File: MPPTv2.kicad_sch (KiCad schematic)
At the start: 11 parts

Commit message: Major
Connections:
- net GND renamed Earth
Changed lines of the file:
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@@
     )
   )
-  (symbol (lib_id "power:GND") (at 129.54 114.3 0) (unit 1)
+  (symbol (lib_id "power:Earth") (at 129.54 114.3 0) (unit 1)
     (in_bom yes) (on_board yes) (dnp no) (fields_autoplaced)
-    (property "Reference" "#PWR?" (at 129.54 120.65 0)
+    (property "Reference" "#PWR01" (at 129.54 120.65 0)
       (effects (font (size 1.27 1.27)) hide)
     )
-    (property "Value" "GND" (at 129.54 119.38 0)
-      (effects (font (size 1.27 1.27)))
+    (property "Value" "Earth" (at 129.54 118.11 0)
+      (effects (font (size 1.27 1.27)) hide)
     )
     (property "Footprint" "" (at 129.54 114.3 0)
       (effects (font (size 1.27 1.27)) hide)
     )
-    (property "Datasheet" "" (at 129.54 114.3 0)
+    (property "Datasheet" "~" (at 129.54 114.3 0)
       (effects (font (size 1.27 1.27)) hide)
     )
     (pin "1")
     (instances
-      (project "FinalBoardCircuits"
-        (path "/7d53e764-a8df-4c50-9cab-d1a3d013fedc/279ce73a-fd26-44c2-9e74-8d0dda75d83d"
-          (reference "#PWR?") (unit 1)
+      (project "pcb"
+        (path "/a8bac665-9e81-4c8d-8e7f-b88478edfeaf/df4161cb-a58b-4c44-b758-adc32db84b1a"
+          (reference "#PWR01") (unit 1)
         )
       )
-      (project "pcb"
-        (path "/a8bac665-9e81-4c8d-8e7f-b88478edfeaf/df4161cb-a58b-4c44-b758-adc32db84b1a"
-          (reference "#PWR03") (unit 1)
-        )
-      )

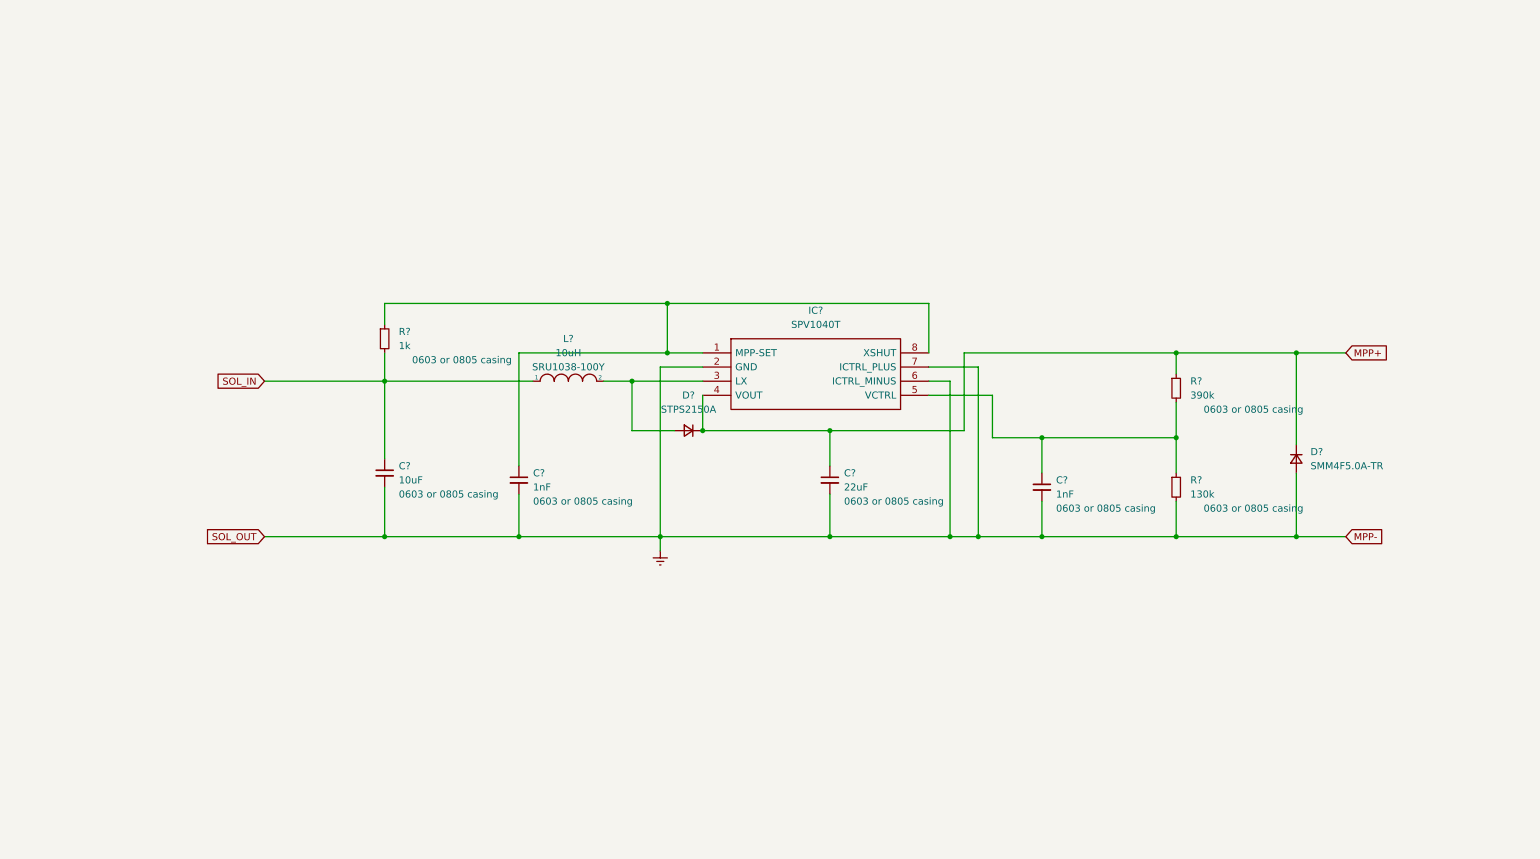
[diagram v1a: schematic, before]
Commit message: Final Schematic
Final Schematic. PC104 pins not assigned.
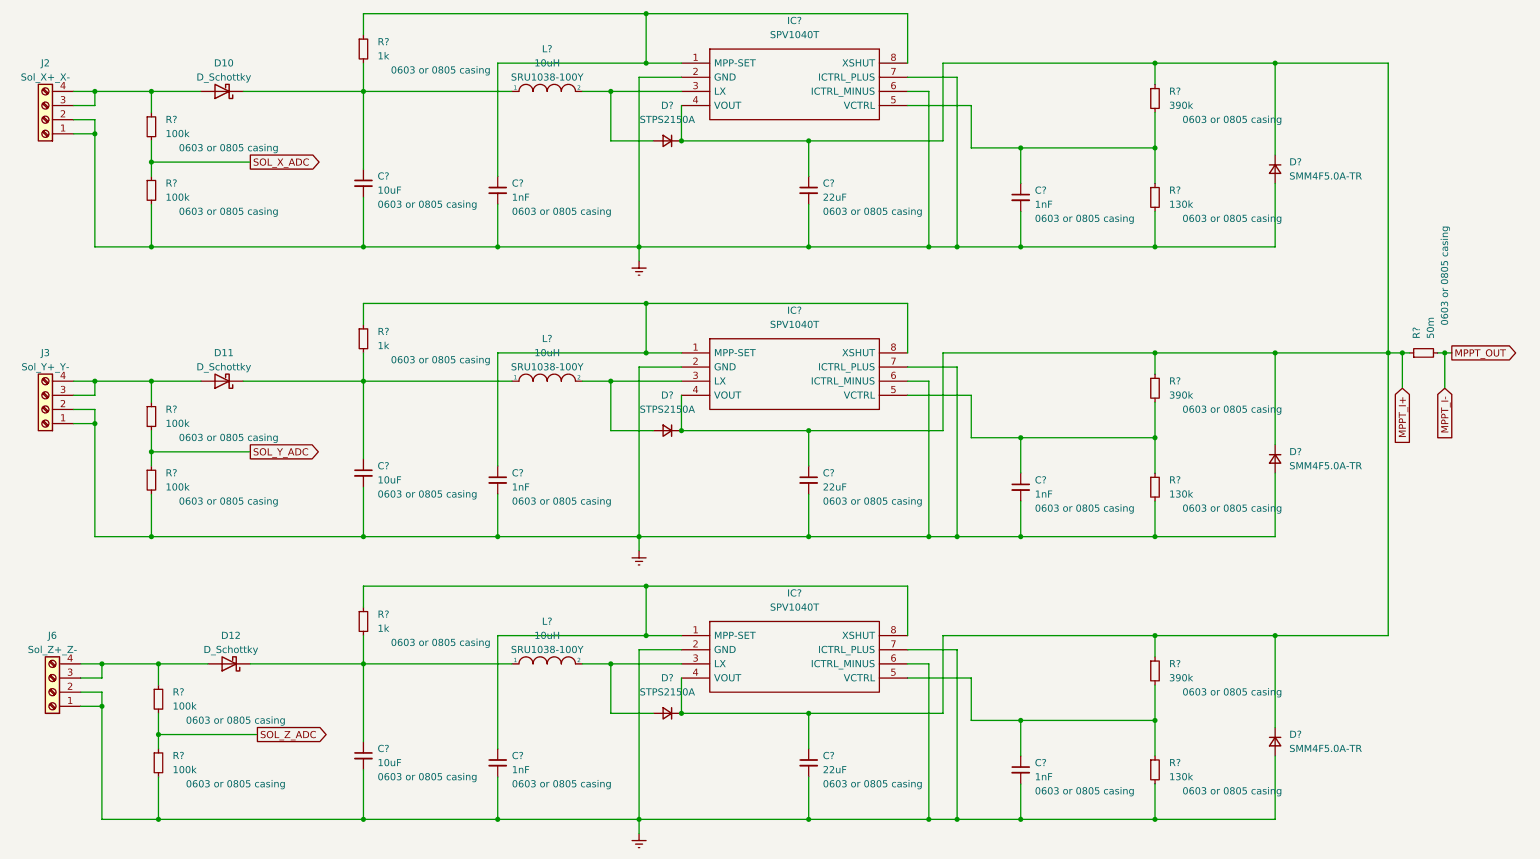
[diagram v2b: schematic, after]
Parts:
- added C? (x2): 10uF, symbol Device:C_Small
- added C? (x4): 1nF, symbol Device:C_Small
- added C? (x2): 22uF, symbol Device:C_Small
- added D10, D11, D12: D_Schottky, symbol Device:D_Schottky
- added D? (x2): STPS2150A, symbol Device:D_Small
- added D? (x2): SMM4F5.0A-TR, symbol Device:D_Small
- added IC? (x2): SPV1040T, myfootprints:SPV1040T, symbol SPV1040T:SPV1040T
- added J2: Sol_X+_X-, symbol Connector:Screw_Terminal_01x04
- added J3: Sol_Y+_Y-, symbol Connector:Screw_Terminal_01x04
- added J6: Sol_Z+_Z-, symbol Connector:Screw_Terminal_01x04
- added L? (x2): 10uH, symbol pspice:INDUCTOR
- added R? (x6): 100k, symbol Device:R_Small
- added R? (x2): 130k, symbol Device:R_Small
- added R? (x2): 390k, symbol Device:R_Small
- added R?: 50m, symbol Device:R_Small
- added R? (x2): 1k, symbol Device:R_Small
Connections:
- net Earth: now also C?.2, C?.2, C?.2, C?.2, C?.2, C?.2, C?.2, C?.2, D?.2 (A), D?.2 (A), IC?.2 (GND), IC?.2 (GND), IC?.6 (ICTRL_MINUS), IC?.6 (ICTRL_MINUS), IC?.7 (ICTRL_PLUS), IC?.7 (ICTRL_PLUS), J2.1 (Pin_1), J2.2 (Pin_2), J3.1 (Pin_1), J3.2 (Pin_2), J6.1 (Pin_1), J6.2 (Pin_2), R?.2, R?.2, R?.2, R?.2, R?.2
- net MPP+ renamed MPPT_I+
- net MPPT_I+: now also C?.1, C?.1, D?.1 (K), D?.1 (K), D?.1 (K), D?.1 (K), IC?.4 (VOUT), IC?.4 (VOUT), R?.1, R?.1, R?.1
- net SOL_IN: no longer names the net of C?.1, L?.1, R?.2
- net SOL_IN: now also D10.1 (K)
- new net: D10.2 (A), J2.3 (Pin_3), J2.4 (Pin_4), R?.1
- new net: D?.2 (A), IC?.3 (LX), L?.2 (x2)
- new net: C?.1, D12.1 (K), L?.1, R?.2
- new net: C?.1, IC?.1 (MPP-SET), IC?.8 (XSHUT), R?.1 (x2)
- new net: C?.1, D11.1 (K), L?.1, R?.2
- new net: D12.2 (A), J6.3 (Pin_3), J6.4 (Pin_4), R?.1
- new net: C?.1, IC?.5 (VCTRL), R?.1, R?.2 (x2)
- new net: D11.2 (A), J3.3 (Pin_3), J3.4 (Pin_4), R?.1
- new net MPPT_I-: R?.2
- new net SOL_X_ADC: R?.1, R?.2
- new net SOL_Y_ADC: R?.1, R?.2
- new net SOL_Z_ADC: R?.1, R?.2
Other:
- moved on the sheet: C?, D?, IC?, L?, R?

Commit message: Ready to rearrange
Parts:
- C? (x6): footprint (none) -> 10uF MLCC:CAPC2012X94N
- C? (x6): footprint (none) -> 47nF:C1005_Commercial
- D10, D11, D12, D? (x6): footprint (none) -> Schottky DD with stock:DIOM5126X265N
- IC? (x3): footprint myfootprints:SPV1040T -> MPPT:SPV1040T
- J2, J3, J6: footprint (none) -> Connector_JST:JST_GH_SM04B-GHS-TB_1x04-1MP_P1.25mm_Horizontal
- L? (x3): footprint (none) -> indc 10uH crct:SRN1060-100M
- R? (x16): footprint (none) -> Resistor_SMD:R_0805_2012Metric

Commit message: LIBS + 3D EXPORT, Ready to reroute
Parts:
- L? (x3): footprint indc 10uH crct:SRN1060-100M -> indc 2.2uH:IHLP2020CZER2R2M8A
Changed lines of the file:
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@@
       (effects (font (size 1.27 1.27)))
     )
-    (property "Footprint" "indc 10uH crct:SRN1060-100M" (at 109.22 83.82 0)
+    (property "Footprint" "indc 2.2uH:IHLP2020CZER2R2M8A" (at 109.22 83.82 0)
       (effects (font (size 1.27 1.27)) hide)
     )
@@
       (effects (font (size 1.27 1.27)))
     )
-    (property "Footprint" "indc 10uH crct:SRN1060-100M" (at 109.22 134.62 0)
+    (property "Footprint" "indc 2.2uH:IHLP2020CZER2R2M8A" (at 109.22 134.62 0)
       (effects (font (size 1.27 1.27)) hide)
     )
@@
       (effects (font (size 1.27 1.27)))
     )
-    (property "Footprint" "indc 10uH crct:SRN1060-100M" (at 109.22 31.75 0)
-      (effects (font (size 1.27 1.27)) hide)
-    )
+    (property "Footprint" "indc 2.2uH:IHLP2020CZER2R2M8A" (at 109.22 31.75 0)
+      (effects (font (size 1.27 1.27)) hide)
+    )
